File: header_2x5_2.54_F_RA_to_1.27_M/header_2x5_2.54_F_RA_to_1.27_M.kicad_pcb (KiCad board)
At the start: 2 copper layers, 18 x 16 mm, 2 parts, among them J1 2.54_F_RA, J2 1.27_M

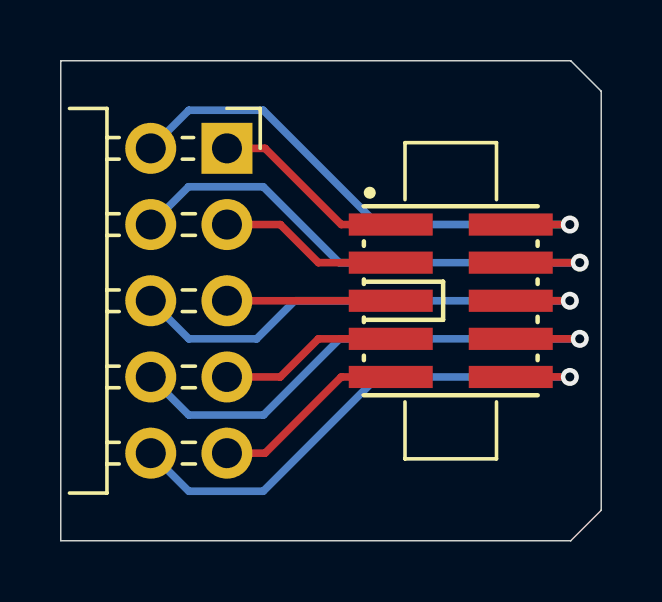
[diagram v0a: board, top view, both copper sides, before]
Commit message: Progress towards 2x5 P2.54mm F RA to P1.27mm M
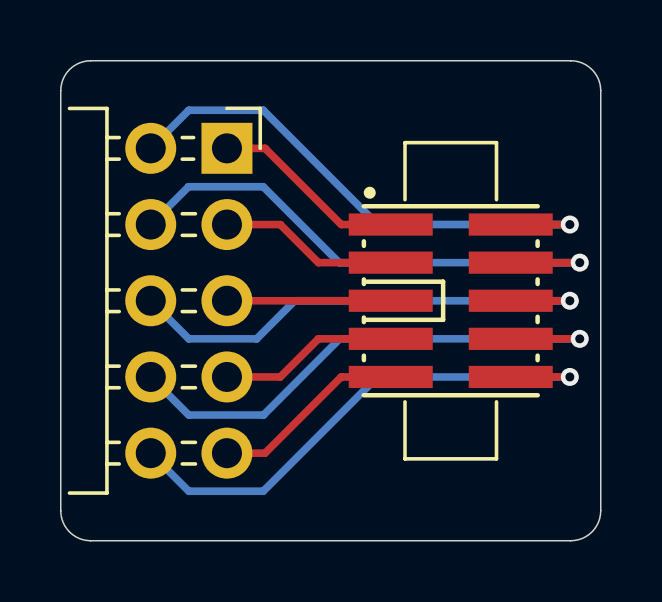
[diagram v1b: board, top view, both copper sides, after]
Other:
- outline, holes or cut-outs redrawn
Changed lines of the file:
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@@
   (general
     (thickness 1.2)
-    (drawings 16)
+    (drawings 18)
     (tracks 45)
     (zones 0)
@@
     )
   )
+  (gr_arc (start 148 107) (end 147 107) (angle -90) (layer Edge.Cuts) (width 0.05))
+  (gr_arc (start 148 93) (end 148 92) (angle -90) (layer Edge.Cuts) (width 0.05))
+  (gr_arc (start 164 107) (end 164 108) (angle -90) (layer Edge.Cuts) (width 0.05))
+  (gr_arc (start 164 93) (end 165 93) (angle -90) (layer Edge.Cuts) (width 0.05))
   (gr_line (start 163.4 106.1) (end 159.4 106.1) (layer B.SilkS) (width 0.12))
   (gr_line (start 163.4 104.8) (end 163.4 106.1) (layer B.SilkS) (width 0.12))
@@
   (gr_line (start 158.2 104.8) (end 158.2 106.1) (layer B.SilkS) (width 0.12))
   (gr_line (start 150 94.92) (end 150 108.5) (layer Dwgs.User) (width 0.1))
-  (gr_line (start 165.016 93.016) (end 165.016 106.984) (layer Edge.Cuts) (width 0.05))
+  (gr_line (start 165 93) (end 165 107) (layer Edge.Cuts) (width 0.05))
   (gr_text "JTAG\nSWD\niCE40" (at 156 106 270) (layer B.SilkS)
     (effects (font (size 0.8 0.8) (thickness 0.15)) (justify left mirror))
   )
-  (gr_line (start 164 92) (end 165.016 93.016) (layer Edge.Cuts) (width 0.05))
-  (gr_line (start 165.016 106.984) (end 164 108) (layer Edge.Cuts) (width 0.05))
   (dimension 16 (width 0.1) (layer Dwgs.User)
     (gr_text "16.000 mm" (at 167 100 90) (layer Dwgs.User)
@@
     (effects (font (size 0.8 0.8) (thickness 0.15)) (justify left mirror))
   )
-  (gr_line (start 164 108) (end 147 108) (layer Edge.Cuts) (width 0.05))
-  (gr_line (start 147 92) (end 164 92) (layer Edge.Cuts) (width 0.05))
-  (gr_line (start 147 92) (end 147 108) (layer Edge.Cuts) (width 0.05))
+  (gr_line (start 164 108) (end 148 108) (layer Edge.Cuts) (width 0.05))
+  (gr_line (start 148 92) (end 164 92) (layer Edge.Cuts) (width 0.05))
+  (gr_line (start 147 93) (end 147 107) (layer Edge.Cuts) (width 0.05))
   (via (at 163.97 102.54) (size 0.6) (drill 0.3) (layers F.Cu B.Cu) (net 1))
   (segment (start 163.97 102.54) (end 162 102.54) (width 0.254) (layer F.Cu) (net 1))
